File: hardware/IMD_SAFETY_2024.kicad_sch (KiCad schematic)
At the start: 10 parts, among them J1 MainConn, J2 SafetyConn, U1 LM393

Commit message: ESF schematic version, relay switched to AXICOM
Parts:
- added C1, C2, C3, C4, C5, C6: 1u/35V, Capacitor_SMD:C_1206_3216Metric, symbol PUTM_EV_IMD_SAFETY_2021-rescue:C-Device
- added C10, C11, C12, C7, C8, C9: 100nF/35V, Capacitor_SMD:C_1206_3216Metric, symbol PUTM_EV_IMD_SAFETY_2021-rescue:C-Device
- added C13: 47uF, symbol PUTM_EV_IMD_SAFETY_2021-rescue:C-Device
- added C14: 22u, symbol Device:C
- added C15: 10u, symbol PUTM_EV_IMD_SAFETY_2021-rescue:C-Device
- added D1: AL5809, symbol Device:D_Constant_Current
- added D2, D4: SD103BW, symbol Device:D_Schottky
- added D3: LED, symbol Device:LED
- added D5: D_TVS, symbol Device:D_TVS
- added D6: D_Small, Diode_SMD:D_SMB, symbol PUTM_EV_IMD_SAFETY_2021-rescue:D_Small-Device
- added JP1: Output_Jumper, Jumper:SolderJumper-2_P1.3mm_Bridged2Bar_Pad1.0x1.5mm, symbol Jumper:SolderJumper_2_Bridged
- added K2: TE AXICOM IM07DTS, footprints:IM23TS, symbol Relay:IM07
- added Q1, Q2: 2N7002, Package_TO_SOT_SMD:SOT-23, symbol PUTM_EV_IMD_SAFETY_2021-rescue:2N7002-Transistor_FET
- added R10, R22: 100k, Resistor_SMD:R_1206_3216Metric, symbol PUTM_EV_IMD_SAFETY_2021-rescue:R-Device
- added R11: 14.3k, Resistor_SMD:R_1206_3216Metric, symbol PUTM_EV_IMD_SAFETY_2021-rescue:R-Device
- added R12: 150K, Resistor_SMD:R_1206_3216Metric, symbol PUTM_EV_IMD_SAFETY_2021-rescue:R-Device
- added R13: 33K, Resistor_SMD:R_1206_3216Metric, symbol PUTM_EV_IMD_SAFETY_2021-rescue:R-Device
- added R14: 0k, Resistor_SMD:R_1206_3216Metric, symbol PUTM_EV_IMD_SAFETY_2021-rescue:R-Device
- added R15: 400K, Resistor_SMD:R_1206_3216Metric, symbol PUTM_EV_IMD_SAFETY_2021-rescue:R-Device
- added R16, R30: 100K, Resistor_SMD:R_1206_3216Metric, symbol PUTM_EV_IMD_SAFETY_2021-rescue:R-Device
- added R17, R18, R29: 2.2K, Resistor_SMD:R_1206_3216Metric, symbol PUTM_EV_IMD_SAFETY_2021-rescue:R-Device
- added R19: 1K, Resistor_SMD:R_1206_3216Metric, symbol PUTM_EV_IMD_SAFETY_2021-rescue:R-Device
- added R20: 10k, Resistor_SMD:R_1206_3216Metric, symbol PUTM_EV_IMD_SAFETY_2021-rescue:R-Device
- added R21: 10k, symbol Device:R_Small
- added R23: 330R, Resistor_SMD:R_1206_3216Metric, symbol PUTM_EV_IMD_SAFETY_2021-rescue:R-Device
- added R24, R27: 20k, symbol Device:R
- added R25: 30k, symbol Device:R
- added R26: 120k, symbol Device:R
- added R28, R31: 10k, symbol Device:R
- added R32: 1M, Resistor_SMD:R_1206_3216Metric, symbol PUTM_EV_IMD_SAFETY_2021-rescue:R-Device
- added R7, R8: 47K, Resistor_SMD:R_1206_3216Metric, symbol PUTM_EV_IMD_SAFETY_2021-rescue:R-Device
- added R9: 300K, Resistor_SMD:R_1206_3216Metric, symbol PUTM_EV_IMD_SAFETY_2021-rescue:R-Device
- added SW1: Push Button, symbol Switch:SW_Push
- added unit 3 of U1
- added U10: 74HCS08, symbol 74xx:74LS08
- added U11, U12, U4, U5: LM393, Package_SO:SO-8_3.9x4.9mm_P1.27mm, symbol PUTM_EV_IMD_SAFETY_2021-rescue:LM393-Comparator
- added U13: 74HC74, symbol 74xx:74HC74
- added U2: 74AC04SC, Package_SO:SOIC-14_3.9x8.7mm_P1.27mm, symbol PUTM_EV_IMD_SAFETY_2021-rescue:74AHC04-74xx
- added U3, U6: 74LVC1G79, Package_TO_SOT_SMD:SOT-23-5, symbol PUTM_EV_IMD_SAFETY_2021-rescue:74LVC1G79-74xGxx
- added U7: MC78M12CDTG, Package_TO_SOT_SMD:TO-252-3_TabPin2, symbol PUTM_EV_IMD_SAFETY_2021-rescue:MC78M05_TO252-Regulator_Linear
- added U8: LM1117IMP-5.0, Package_TO_SOT_SMD:SOT-223-3_TabPin2, symbol PUTM_EV_IMD_SAFETY_2021-rescue:LM1117-5.0-Regulator_Linear
- added U9: 74HCS32, Package_SO:SOIC-14_3.9x8.7mm_P1.27mm, symbol PUTM_EV_IMD_SAFETY_2021-rescue:74LS32-74xx
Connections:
- net +24V: now also C12.1, C3.1, D5.2 (A2), D6.1 (K), K2.1, U5.8 (V+), U7.1 (VI)
- net +5V: now also C10.1, C11.1, C14.1, C6.1, C7.1, C8.1, C9.1, D1.2 (A), K2.3, R15.2, R17.1, R18.1, R24.1, R28.1, R29.1, R31.1, R9.2, U1.8 (V+), U2.14 (VCC), U3.5 (VCC), U4.8 (V+), U6.5 (VCC), U8.2 (VO), U9.14 (VCC)
- net COCKPIT_LED: now also Q2.1 (G), R21.1, R23.1
- net GND: now also C1.2, C10.2, C11.2, C12.2, C13.2, C15.2, C2.2, C3.2, C4.2, C5.2, C6.2, C7.2, C8.2, C9.2, D3.1 (K), D5.1 (A1), Q1.2 (S), Q2.2 (S), R14.1, R19.1, R20.1, R21.2, R25.2, R26.2, R32.1, SW1.1, U1.4 (V-), U2.7 (GND), U3.3 (GND), U4.4 (V-), U5.4 (V-), U6.3 (GND), U7.2 (GND), U8.1 (GND), U9.7 (GND)
- net OK_HS_TTL: now also U9.1
- net PWM_TTL: now also U2.3, U3.2 (C)
- net EXT_RESET renamed RESET
- net RESET: now also R27.2, R28.2, SW1.2, U12.1, U13.3 (C)
- net SAFETY_IN renamed SDC_IN
- net SDC_IN: now also K2.6
- net SAFETY_OUT renamed SDC_OUT
- net SDC_OUT: now also K2.5
- new net: R15.1, R16.2, U5.3 (+)
- new net: D1.1 (K), D3.2 (A), Q2.3 (D)
- new net: R12.1, R13.2, U5.6 (_)
- new net: R11.1, R12.2
- new net: R31.2, U13.2 (D), U13.4 (~{S})
- new net: D4.2 (A), R29.2, R30.1, U9.3
- new net: C15.1, D4.1 (K), R30.2, U13.1 (~{R})
- new net: R10.2, R9.1
- new net: C2.1, R8.1, U4.2 (-), U5.5 (+)
- new net: R17.2, U4.1, U5.7, U6.1 (D)
- new net: U2.4, U2.5
- new net: R7.2, U2.6
- new net: R13.1, R14.2
- new net: D6.2 (A), K2.8, Q1.3 (D)
- new net: C14.2, R26.1, U12.2 (-)
- new net: C1.1, R7.1, U11.3 (+), U5.2 (-)
- new net: R10.1, R11.2, U4.3 (+)
- new net: K2.4, R23.2
- new net: R16.1, R19.2, U11.2 (-)
- new net: U2.2, U3.1 (D)
- new net: R8.2, U2.1, U3.4 (Q), U6.2 (C)
- new net: R24.2, R25.1, R27.1, U12.3 (+)
- new net: U10.3, U9.2
- new net +12V: C4.1, C5.1, U7.3 (VO), U8.3 (VI)
- new net DUTY_OK: R18.2, U10.1, U11.1, U5.1
- new net NMOS_IN: C13.1, D2.2 (A), JP1.2 (B), Q1.1 (G), R20.2, R22.1, R32.2
- new net PWM_FREQ_OK: U10.2, U6.4 (Q)
- new net Q_DFF: D2.1 (K), JP1.1 (A), R22.2, U13.5 (Q)
- no-connect marks 0 -> 3
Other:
- note added: "'0' WHEN > 1V ON RISING OF PWM"
- note added: "1.0V"
- note added: "AND functionality by Open Drain outputs"
- note added: "Additional manual reset button outside of drivers reach ->"
- note added: "CHECK IF SIGNAL IS PRESENT IF DUTY >0.05V"
- note added: "Cockpit LED PCB side"
- note added: "Decision Logic, SDC Latch"
- note added: "Duty Check"
- note added: "ERR"
- note added: "FREQ DIVIDER OUTPUT DUTY ALWAYS 50%"
- note added: "Frequency Check"
- note added: "Legacy RC hold. Populate only if turns out nescessary"
- note added: "OK"
- note added: "Only on the rising edge of 74HC74 CLK (Auto-Reset or Reset Button) Q output will assert IMD OK signal from CLR input, if signal is not present it latches low"
- note added: "SCS"
- note added: "Supply Section"
- note added: "WHEN RISING EDGE OF PWM, THE VOLTAGE LEVEL FOR 10HZ-30HZ IS BEETWEN 0.5V AND 2V"
- note added: "turns LED OFF when closing SDC by MOSFET bypass, safe state is LED ON"
- note added: "~2.7s Autoreset delay"
- company: Author: -> Author: Przemysław Zioła
- title: (none) -> IMD Shutdown Circuit Logic
- moved on the sheet: F1, J1, R1, R2

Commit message: IC footprints assign
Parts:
- removed J2: SafetyConn, Connector_Molex:Molex_Micro-Fit_3.0_43650-0200_1x02_P3.00mm_Horizontal, symbol PUTM_EV_IMD_SAFETY_2021-rescue:Conn_01x02-Connector_Generic
- removed U1, U11, U12, U4, U5: LM393, Package_SO:SO-8_3.9x4.9mm_P1.27mm, symbol PUTM_EV_IMD_SAFETY_2021-rescue:LM393-Comparator
- added C16, C17, C18: 100nF/35V, Capacitor_SMD:C_1206_3216Metric, symbol PUTM_EV_IMD_SAFETY_2021-rescue:C-Device
- added U1: LM393, symbol Comparator:LM393
- added unit 5 of U10
- added unit 3 of U13
- added U14, U15, U16: LM393, Samacsys:SOP65P640X120-8N, symbol Comparator:LM393
- C13: footprint (none) -> Capacitor_SMD:C_1206_3216Metric; Mouser# (none) -> 187-CL31A476MQHNNNE
- C15: footprint (none) -> Capacitor_SMD:C_1206_3216Metric; Mouser# (none) -> 187-CL31A106MQHNNNE
- D2: Mouser# (none) -> 637-SD103BW
- D4: footprint (none) -> Diode_SMD:D_SOD-123F; Mouser# (none) -> 637-SD103BW
- D5: value D_TVS -> SD24-01FTG; footprint (none) -> Samacsys:SOD2613X114N
- D6: value D_Small -> SK36A-LTP; footprint Diode_SMD:D_SMB -> Samacsys:DIOM5226X244N; Mouser# (none) -> 833-SK36A-LTP
- F1: value Fuse -> 500mA; footprint Fuse:Fuse_1812_4532Metric -> Fuse:Fuse_1206_3216Metric; Mouser# (none) -> 667-ERB-RG0R50V
- J1: value MainConn -> Main- M80-5300842; footprint Connector_Molex:Molex_Micro-Fit_3.0_43650-0600_1x06_P3.00mm_Horizontal -> Samacsys:M80-53008YY; symbol PUTM_EV_IMD_SAFETY_2021-rescue:Conn_01x06-Connector_Generic -> Connector_Generic:Conn_01x08
- R20: footprint Resistor_SMD:R_1206_3216Metric -> Resistor_SMD:R_0603_1608Metric
- U10: footprint (none) -> Samacsys:SOP65P640X120-14N; Mouser# (none) -> 595-SN74HCS08PWR
- U13: footprint (none) -> Samacsys:SOP65P640X120-14N
- U2: Mouser# (none) -> 512-74AC04SC
- U3, U6: Mouser# (none) -> 595-SN74LVC1G79DBVR
- U7: Mouser# (none) -> 863-MC7812ACD2TR4G
- U8: Mouser# (none) -> 926-LM1117IMPX50NOPB
- U9: footprint Package_SO:SOIC-14_3.9x8.7mm_P1.27mm -> Samacsys:SOP65P640X120-14N; Mouser# (none) -> 595-SN74HCS32PWR
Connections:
- net +24V: now also C16.1, U1.8 (V+), U16.8 (V+)
- net +5V: now also C17.1, C18.1, U10.14 (VCC), U13.14 (VCC), U14.8 (V+), U15.8 (V+)
- net DUTY_OK: now also U15.1, U15.7
- net GND: now also C16.2, C17.2, C18.2, U1.4 (V-), U10.7 (GND), U13.7 (GND), U14.4 (V-), U15.4 (V-), U16.4 (V-)
- net IMD_OK_HS: now also J1.3 (Pin_3), U14.3 (+); no longer J1.2 (Pin_2)
- net IMD_PWM_LS: now also J1.2 (Pin_2), U14.5 (+); no longer J1.3 (Pin_3)
- net OK_HS_TTL: now also U14.1
- net PWM_TTL: now also U14.7
- net RESET: now also U1.1
- net SDC_IN: now also J1.7 (Pin_7)
- net SDC_OUT: now also J1.8 (Pin_8)
- net at R15.1, R16.2: now also U15.3 (+)
- net at R12.1, R13.2: now also U16.6 (-)
- net at C2.1, R8.1: now also U16.2 (-), U16.5 (+)
- net at R17.2, U6.1 (D): now also U16.1, U16.7
- net at R3.2, R4.1: now also U14.2 (-), U14.6 (-)
- net at C14.2, R26.1: now also U1.2 (-)
- net at C1.1, R7.1: now also U15.2 (-), U15.5 (+)
- net at R10.1, R11.2: now also U16.3 (+)
- net at R16.1, R19.2: now also U15.6 (-)
- net at R24.2, R25.1, R27.1: now also U1.3 (+)
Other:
- note added: "Connector"
- note added: "Mating connectors: M80-4130898 M80-4140898"
- note removed: "Connectors"
- moved on the sheet: C10, C11, C12, C3, C4, C5, C6, C7, C8, C9, U2G, U7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

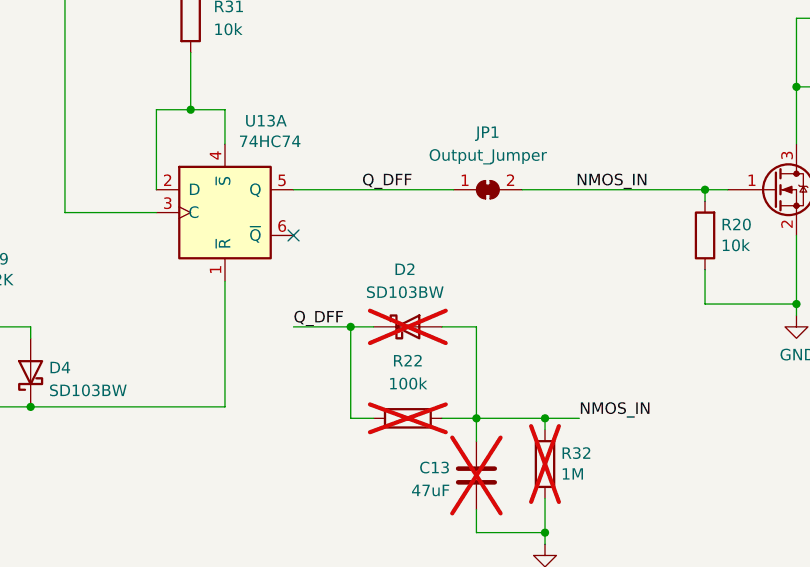
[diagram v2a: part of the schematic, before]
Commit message: Passives footprint assignment
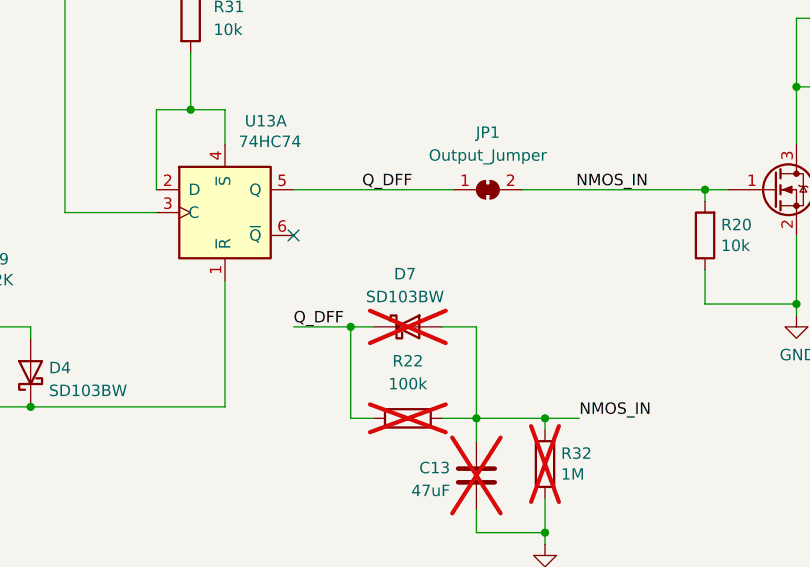
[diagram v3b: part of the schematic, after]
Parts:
- removed D2: SD103BW, symbol Device:D_Schottky
- added D7: SD103BW, Diode_SMD:D_SOD-123F, symbol Device:D_Schottky
- C1, C2, C3, C4, C5, C6: footprint Capacitor_SMD:C_1206_3216Metric -> Capacitor_SMD:C_0805_2012Metric
- C10, C11, C12, C16, C17, C18, C7, C8, C9: footprint Capacitor_SMD:C_1206_3216Metric -> Capacitor_SMD:C_0603_1608Metric
- C14: footprint (none) -> Capacitor_SMD:C_1206_3216Metric; Mouser# (none) -> 187-CL31A226KOHNNWE
- Q1: Mouser# (none) -> 726-2N7002H6327XTSA2
- R1, R10, R11, R12, R13, R14, R15, R16, R17, R18, R19, R2, R22, R23, R29, R3, R30, R32, R4, R5, R6, R7, R8, R9: footprint Resistor_SMD:R_1206_3216Metric -> Resistor_SMD:R_0603_1608Metric
- R24, R25, R26, R27, R28, R31: footprint (none) -> Resistor_SMD:R_0603_1608Metric
- U1: footprint (none) -> Samacsys:SOIC127P600X175-8N; Mouser# (none) -> 595-LM393ADR
- U14, U15, U16: footprint Samacsys:SOP65P640X120-8N -> Samacsys:SOIC127P600X175-8N; Mouser# (none) -> 595-LM393ADR
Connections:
- net NMOS_IN: now also D7.2 (A)
- net Q_DFF: now also D7.1 (K)

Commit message: WIP Layout
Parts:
- added C19, C20: 100nF/35V, Capacitor_SMD:C_0603_1608Metric, symbol PUTM_EV_IMD_SAFETY_2021-rescue:C-Device
- added C21: TBD, Capacitor_SMD:C_1206_3216Metric, symbol Device:C
- added TP1, TP10, TP11, TP12, TP13, TP14, TP15, TP2, TP3, TP4, TP5, TP6, TP7, TP8, TP9: TestPoint_Small, TestPoint:TestPoint_Pad_D1.0mm, symbol Connector:TestPoint_Small
- JP1: footprint Jumper:SolderJumper-2_P1.3mm_Bridged2Bar_Pad1.0x1.5mm -> Jumper:SolderJumper-2_P1.3mm_Open_Pad1.0x1.5mm
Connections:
- net +24V: no longer C12.1, C16.1, U1.8 (V+), U16.8 (V+)
- net +5V: now also C12.1, C16.1, U1.8 (V+), U16.8 (V+), C19.1, C20.1, C21.1
- net COCKPIT_LED: now also J1.6 (Pin_6); no longer J1.5 (Pin_5)
- net GND: now also J1.5 (Pin_5), C19.2, C20.2; no longer J1.6 (Pin_6)
- net IMD_OK_HS: now also TP2.1
- net IMD_PWM_LS: now also TP1.1
- net PWM_TTL: now also TP9.1
- net at R15.1, R16.2, U15.3 (+): now also TP6.1
- net at R12.1, R13.2, U16.6 (-): now also TP14.1
- net ~{CLR}: now reaches C15.1, D4.1 (K), R30.2, U13.1 (~{R})
- net at R7.2, U2.6: now also TP5.1
- net at C14.2, R26.1, U1.2 (-): now also C21.2, TP3.1
- net at C1.1, R7.1, U15.2 (-)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: now also TP7.1
- net at C2.1, R8.1, U16.2 (-)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: now also TP12.1
- net at R16.1, R19.2, U15.6 (-): now also TP8.1
- net at U2.2, U3.1 (D): now also TP10.1
- net at R8.2, U2.1, U3.4 (Q)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: now also TP11.1
- net at R24.2, R25.1, R27.1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: now also TP4.1
- net at R10.1, R11.2, U16.3 (+): now also TP13.1
- net at R17.2, U16.1, U16.7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: now also TP15.1
- net DUTY&FREQ_OK: now reaches U10.3, U9.2
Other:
- added sheet Unused inputs (unused.kicad_sch)
- note added: "C21 is spare footprint for fine-tuning reset delay"
- note added: "DFF's power decoupling"
- moved on the sheet: C10, C11, C12, C13, C15, C16, C17, C18, C8, C9, D4, D6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

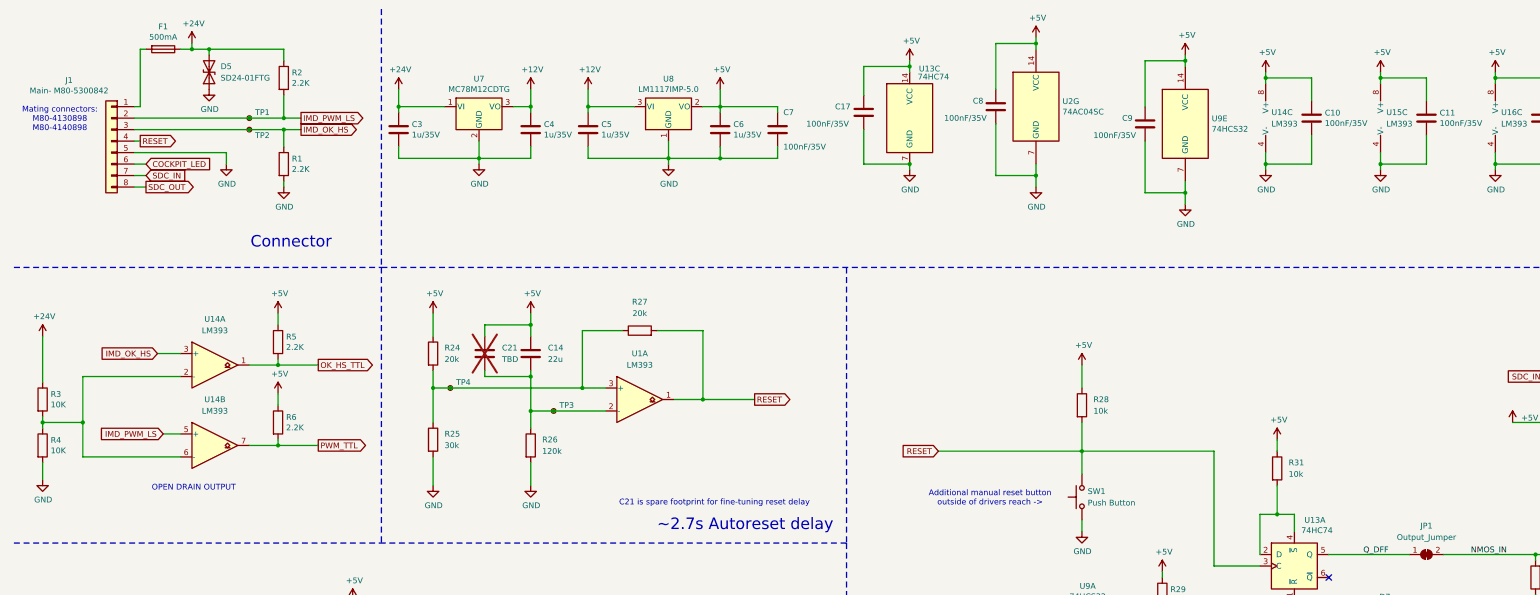
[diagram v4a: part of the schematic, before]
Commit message: Updated R3 R4 Values
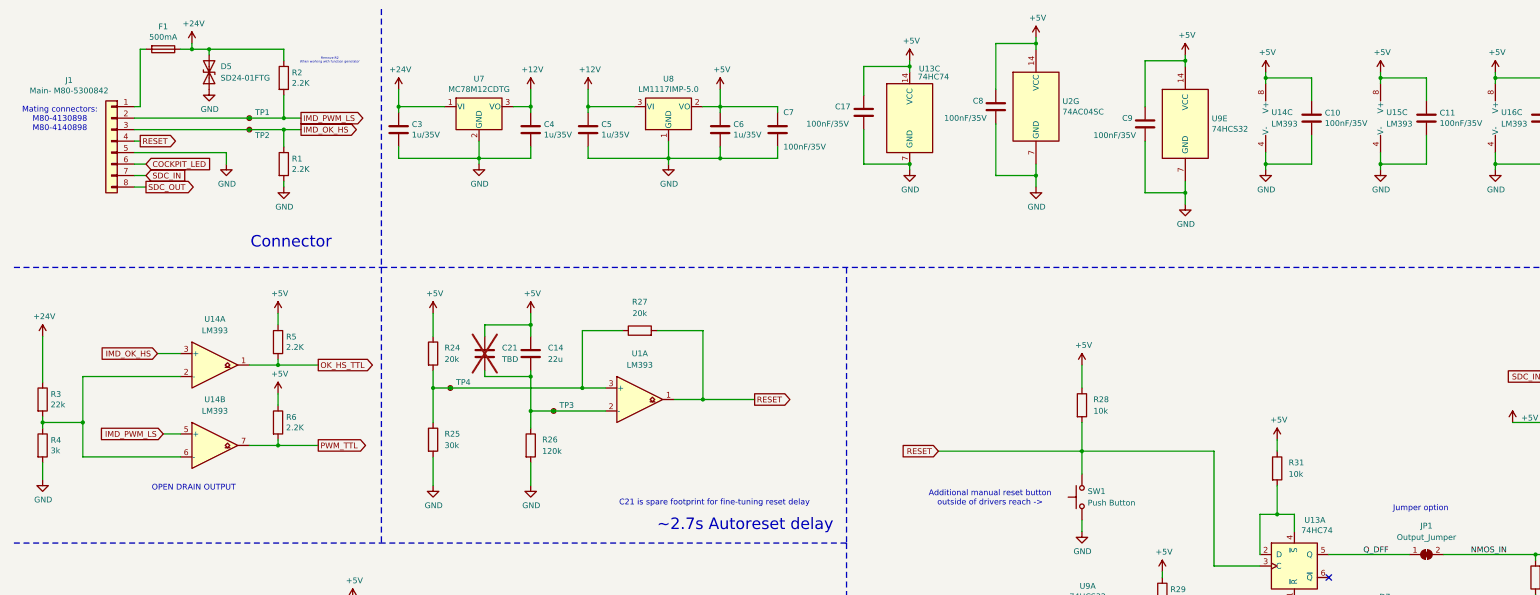
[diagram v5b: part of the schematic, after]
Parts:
- R3: value 10K -> 22k
- R4: value 10K -> 3k
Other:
- note added: "Jumper option"
- note added: "Remove R2 When working with function generator"
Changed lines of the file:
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@@
 		)
 	)
+	(text "Remove R2\nWhen working with function generator"
+		(exclude_from_sim no)
+		(at 82.55 24.13 0)
+		(effects
+			(font
+				(size 0.5 0.5)
+			)
+		)
+	)
 	(text "Cockpit LED PCB side"
 		(exclude_from_sim no)
@@
 		)
 	)
+	(text "Jumper option\n"
+		(exclude_from_sim no)
+		(at 323.85 123.19 0)
+		(effects
+			(font
+				(size 1.27 1.27)
+			)
+		)
+	)
 	(text "Supply Section"
 		(exclude_from_sim no)
@@
 			)
 		)
-		(property "Value" "10K"
+		(property "Value" "3k"
 			(at 20.828 110.363 0)
 			(effects
@@
 			)
 		)
-		(property "Value" "10K"
+		(property "Value" "22k"
 			(at 20.828 100.203 0)
 			(effects

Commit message: FSG fuckup comment
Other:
- note added: "///FSG REGULATED"
- note added: "100Ohms"
- note added: "100kOhm"
- note added: "2.7kOhms"
- note added: "3,455"
- note added: "5kOhms"
- note added: "DODAĆ DIODE"
- note added: "DODAĆ TVS, CAP 100nF i 100R"
- note added: "NEEEDED THRESHOLD 3,26V - 65% DUTY - 600 kOhms"
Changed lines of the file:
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@@
+		)
+	)
+	(text "100Ohms"
+		(exclude_from_sim no)
+		(at 93.98 177.8 0)
+		(effects
+			(font
+				(size 1.27 1.27)
+			)
 		)
 	)
@@
 		)
 	)
+	(text "///FSG REGULATED"
+		(exclude_from_sim no)
+		(at 69.85 152.4 0)
+		(effects
+			(font
+				(size 1.27 1.27)
+			)
+		)
+	)
 	(text "Decision Logic, SDC Latch"
 		(exclude_from_sim no)
@@
 		)
 	)
+	(text "5kOhms"
+		(exclude_from_sim no)
+		(at 80.01 157.48 0)
+		(effects
+			(font
+				(size 1.27 1.27)
+			)
+		)
+	)
 	(text "~2.7s Autoreset delay"
 		(exclude_from_sim no)
@@
 		)
 	)
+	(text "2.7kOhms"
+		(exclude_from_sim no)
+		(at 78.74 147.32 0)
+		(effects
+			(font
+				(size 1.27 1.27)
+			)
+		)
+	)
 	(text "DFF's power decoupling"
 		(exclude_from_sim no)
@@
 		)
 	)
+	(text "DODAĆ TVS, CAP 100nF i 100R"
+		(exclude_from_sim no)
+		(at 233.68 116.84 0)
+		(effects
+			(font
+				(size 1.27 1.27)
+			)
+		)
+	)
 	(text "Frequency Check"
 		(exclude_from_sim no)
@@
 		)
 	)
+	(text "3,455\n"
+		(exclude_from_sim no)
+		(at 176.53 144.78 0)
+		(effects
+			(font
+				(size 1.27 1.27)
+			)
+		)
+	)
 	(text "Jumper option\n"
 		(exclude_from_sim no)
@@
 		)
 	)
+	(text "100kOhm\n"
+		(exclude_from_sim no)
+		(at 172.72 157.48 0)
+		(effects
+			(font
+				(size 1.27 1.27)
+			)
+		)
+	)
 	(text "Supply Section"
 		(exclude_from_sim no)
@@
 		)
 	)
+	(text "DODAĆ DIODE"
+		(exclude_from_sim no)
+		(at 392.43 97.79 0)
+		(effects
+			(font
+				(size 1.27 1.27)
+			)
+		)
+	)
 	(text "Duty Check"
 		(exclude_from_sim no)
@@
 		)
 	)
+	(text "NEEEDED THRESHOLD 3,26V - 65% DUTY - 600 kOhms "
+		(exclude_from_sim no)
+		(at 57.15 140.97 0)
+		(effects
+			(font
+				(size 1.27 1.27)
+			)
+		)
+	)
 	(text "SCS"
 		(exclude_from_sim no)
@@
 	(text "1.0V"
 		(exclude_from_sim no)
-		(at 82.55 153.67 0)
-		(effects
-			(font
+		(at 95.25 160.02 0)
+		(effects
+			(font
